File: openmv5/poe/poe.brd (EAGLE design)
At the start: 35.6 x 44.4 mm, 51 parts, among them IC1 AG9905LP, J1 GMJXHT-MM-S-88, J2 OPENMV5-BOTTOM, T1 PT61018PEL

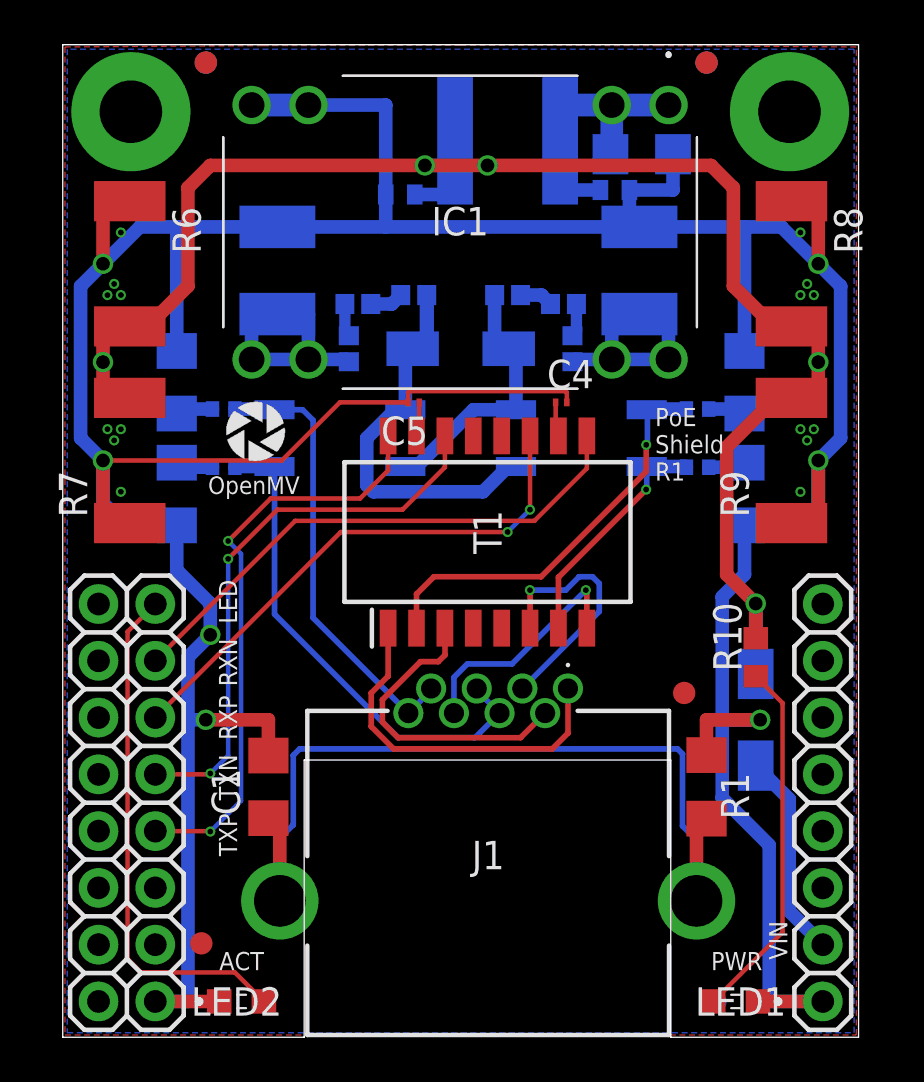
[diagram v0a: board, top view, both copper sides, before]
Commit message: Add CAN/RS232 shield
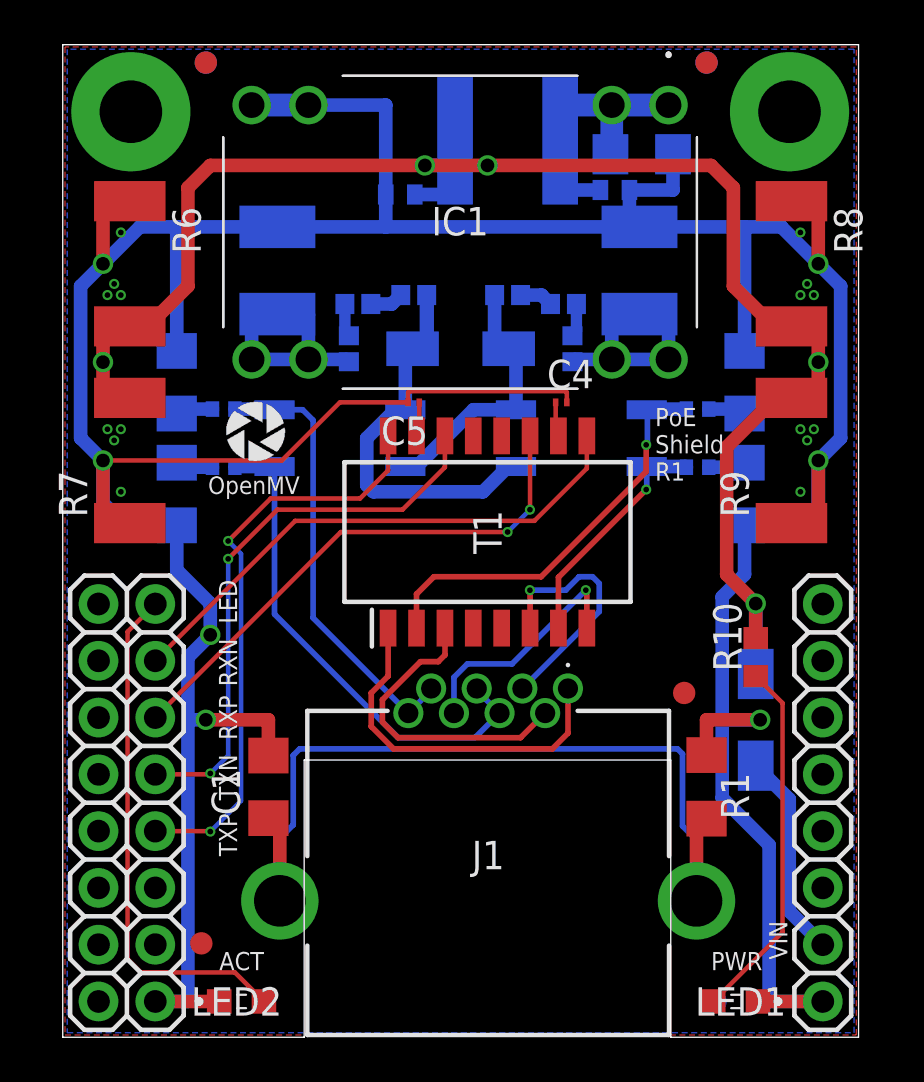
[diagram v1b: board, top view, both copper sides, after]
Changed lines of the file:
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@@
 <vertex x="0.1" y="0.1"/>
 <vertex x="35.5" y="0.1"/>
-<vertex x="35.5" y="44.3" curve="1.012964"/>
+<vertex x="35.5" y="44.3"/>
 <vertex x="0.1" y="44.3"/>
 </polygon>

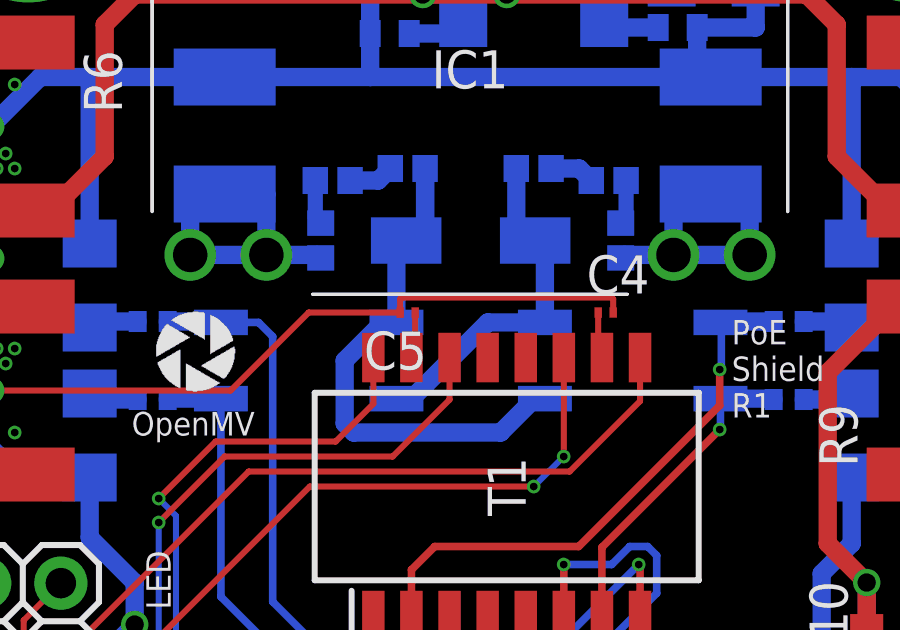
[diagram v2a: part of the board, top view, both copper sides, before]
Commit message: Remove 0201 components
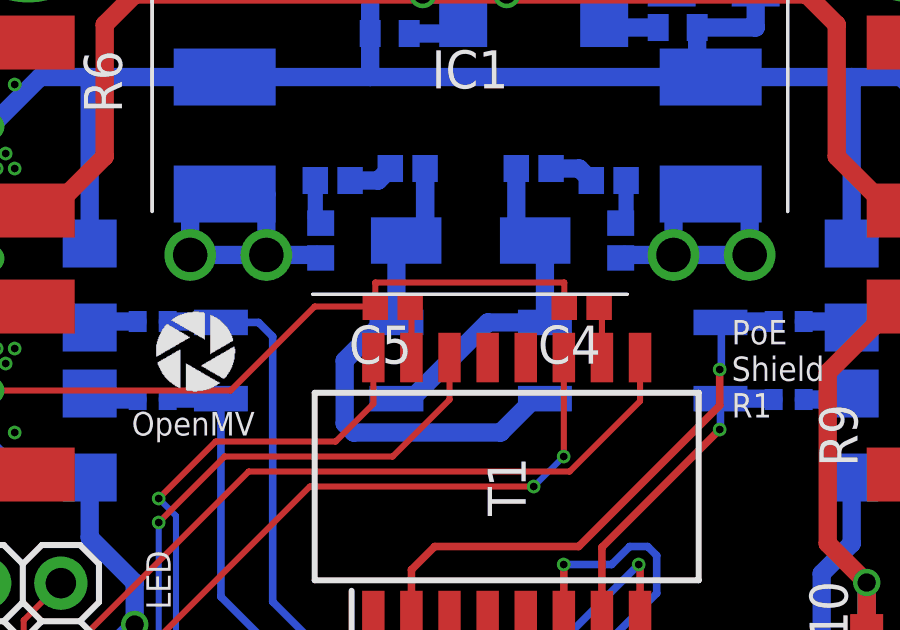
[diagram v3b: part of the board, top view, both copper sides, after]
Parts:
- C4, C5: device rcl:C0201 -> SparkFun-Capacitors:0402
- moved C4 0.82 mm to (21.5, 28.6), turned to 180 degrees
- moved C5 0.54 mm to (15.2, 28.6)
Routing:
- net GND: track 196.3 -> 195.4 mm
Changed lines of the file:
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@@
 <attribute name="VALUE" x="19" y="22.6" size="1.27" layer="27" rot="R90" align="center"/>
 </element>
-<element name="C5" library="rcl" library_urn="urn:adsk.eagle:library:334" package="C0201" package3d_urn="urn:adsk.eagle:package:23690/2" value="0.1uF" x="15.7" y="28.4" smashed="yes" rot="R180">
-<attribute name="MPN" value="CL03A104KQ3NNNC" x="15.7" y="28.4" size="1.778" layer="27" rot="R180" display="off"/>
-<attribute name="NAME" x="16.335" y="27.765" size="1.27" layer="25" rot="R180"/>
-<attribute name="POPULARITY" value="0" x="15.7" y="28.4" size="1.778" layer="27" rot="R180" display="off"/>
-<attribute name="SPICEPREFIX" value="C" x="15.7" y="28.4" size="1.778" layer="27" rot="R180" display="off"/>
-<attribute name="VALUE" x="16.335" y="30.305" size="1.27" layer="27" rot="R180"/>
-</element>
-<element name="C4" library="rcl" library_urn="urn:adsk.eagle:library:334" package="C0201" package3d_urn="urn:adsk.eagle:package:23690/2" value="0.1uF" x="22.3" y="28.4" smashed="yes">
-<attribute name="MPN" value="CL03A104KQ3NNNC" x="22.3" y="28.4" size="1.778" layer="27" display="off"/>
-<attribute name="NAME" x="21.665" y="29.035" size="1.27" layer="25"/>
-<attribute name="POPULARITY" value="0" x="22.3" y="28.4" size="1.778" layer="27" display="off"/>
-<attribute name="SPICEPREFIX" value="C" x="22.3" y="28.4" size="1.778" layer="27" display="off"/>
-<attribute name="VALUE" x="21.665" y="26.495" size="1.27" layer="27"/>
+<element name="C5" library="SparkFun-Capacitors" library_urn="urn:adsk.eagle:library:510" package="0402" package3d_urn="urn:adsk.eagle:package:37413/1" value="0.1uF" x="15.2" y="28.6" smashed="yes" rot="R180">
+<attribute name="MPN" value="GRM155R71H104KE14D" x="15.2" y="28.6" size="1.778" layer="27" rot="R180" display="off"/>
+<attribute name="NAME" x="15.835" y="27.965" size="1.27" layer="25" rot="R180"/>
+<attribute name="PROD_ID" value="CAP-12416" x="15.2" y="28.6" size="1.778" layer="27" rot="R180" display="off"/>
+<attribute name="VALUE" value="0.1uF" x="15.835" y="30.505" size="1.27" layer="27" rot="R180"/>
+</element>
+<element name="C4" library="SparkFun-Capacitors" library_urn="urn:adsk.eagle:library:510" package="0402" package3d_urn="urn:adsk.eagle:package:37413/1" value="0.1uF" x="21.5" y="28.6" smashed="yes" rot="R180">
+<attribute name="MPN" value="GRM155R71H104KE14D" x="21.5" y="28.6" size="1.778" layer="27" rot="R180" display="off"/>
+<attribute name="NAME" x="22.135" y="27.965" size="1.27" layer="25" rot="R180"/>
+<attribute name="PROD_ID" value="CAP-12416" x="21.5" y="28.6" size="1.778" layer="27" rot="R180" display="off"/>
+<attribute name="VALUE" value="0.1uF" x="22.135" y="30.505" size="1.27" layer="27" rot="R180"/>
 </element>
 <element name="BR1" library="MB6S-TP" package="SOP254P665X270-4N" value="MB6S-TP" x="23.2" y="26.8" smashed="yes" rot="MR0">
@@
 <wire x1="29.5" y1="10.7" x2="31.6" y2="8.6" width="0.6096" layer="16"/>
 <wire x1="1.8" y1="25.8" x2="9.8" y2="25.8" width="0.2032" layer="1"/>
-<wire x1="9.8" y1="25.8" x2="12.4" y2="28.4" width="0.2032" layer="1"/>
-<wire x1="12.4" y1="28.4" x2="15.45" y2="28.4" width="0.2032" layer="1"/>
-<wire x1="22.55" y1="28.4" x2="22.55" y2="28.85" width="0.2032" layer="1"/>
-<wire x1="22.55" y1="28.85" x2="22.5" y2="28.9" width="0.2032" layer="1"/>
-<wire x1="22.5" y1="28.9" x2="15.5" y2="28.9" width="0.2032" layer="1"/>
-<wire x1="15.45" y1="28.85" x2="15.45" y2="28.4" width="0.2032" layer="1"/>
-<wire x1="15.5" y1="28.9" x2="15.45" y2="28.85" width="0.2032" layer="1"/>
+<wire x1="9.8" y1="25.8" x2="12.6" y2="28.6" width="0.2032" layer="1"/>
+<wire x1="12.6" y1="28.6" x2="14.62" y2="28.6" width="0.2032" layer="1"/>
+<wire x1="20.92" y1="28.6" x2="20.92" y2="29.4" width="0.2032" layer="1"/>
+<wire x1="20.92" y1="29.4" x2="14.62" y2="29.4" width="0.2032" layer="1"/>
+<wire x1="14.62" y1="28.6" x2="14.62" y2="29.4" width="0.2032" layer="1"/>
 <via x="6.6" y="18" extent="1-16" drill="0.6096"/>
 <contactref element="C1" pad="2"/>
@@
 <contactref element="T1" pad="15"/>
 <contactref element="C5" pad="1"/>
-<wire x1="15.95" y1="28.4" x2="15.95" y2="27.025" width="0.2032" layer="1"/>
-<wire x1="15.95" y1="27.025" x2="15.825" y2="26.9" width="0.2032" layer="1"/>
+<wire x1="15.78" y1="28.6" x2="15.625" y2="28.6" width="0.2032" layer="1"/>
+<wire x1="15.825" y1="26.9" x2="15.825" y2="28.4" width="0.2032" layer="1"/>
+<wire x1="15.825" y1="28.4" x2="15.625" y2="28.6" width="0.2032" layer="1"/>
 </signal>
 <signal name="MDI_RX_CT" class="3">
 <contactref element="T1" pad="10"/>
 <contactref element="C4" pad="1"/>
-<wire x1="22.05" y1="28.4" x2="22.05" y2="27.025" width="0.2032" layer="1"/>
-<wire x1="22.05" y1="27.025" x2="22.175" y2="26.9" width="0.2032" layer="1"/>
+<wire x1="22.08" y1="28.6" x2="22.063075" y2="28.616925" width="0.2032" layer="1"/>
+<wire x1="22.063075" y1="28.616925" x2="22.057625" y2="28.617375" width="0.2032" layer="1"/>
+<wire x1="22.175" y1="28.5" x2="22.175" y2="26.9" width="0.2032" layer="1"/>
+<wire x1="22.175" y1="28.5" x2="22.057625" y2="28.617375" width="0.2032" layer="1"/>
 </signal>
 <signal name="TX_N" class="4">

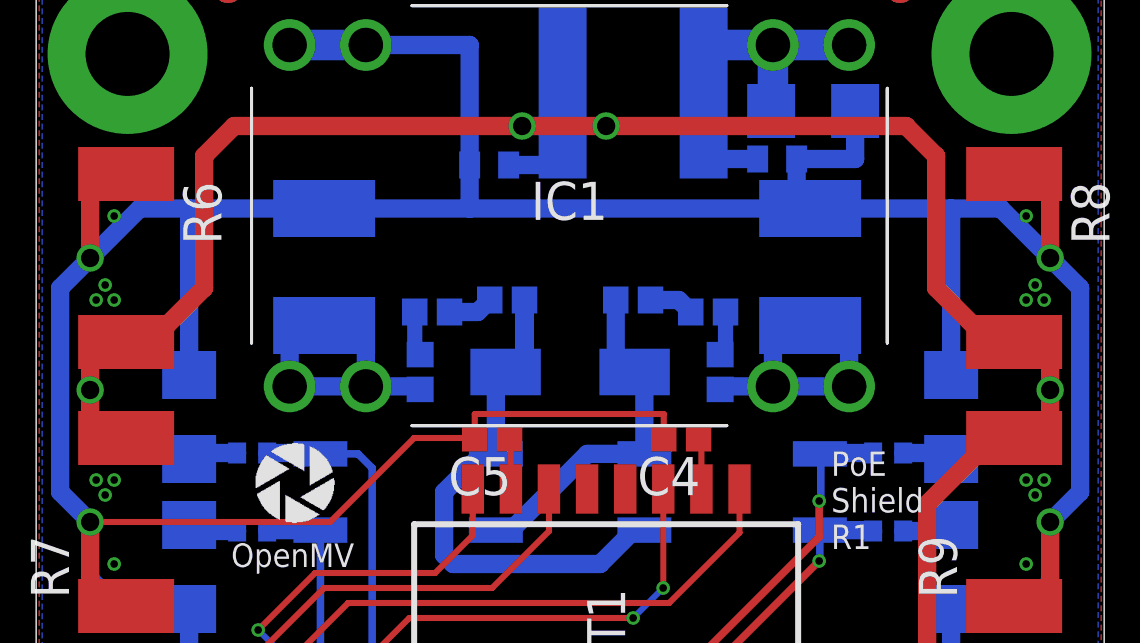
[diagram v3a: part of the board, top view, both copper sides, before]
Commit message: Fix inductor size
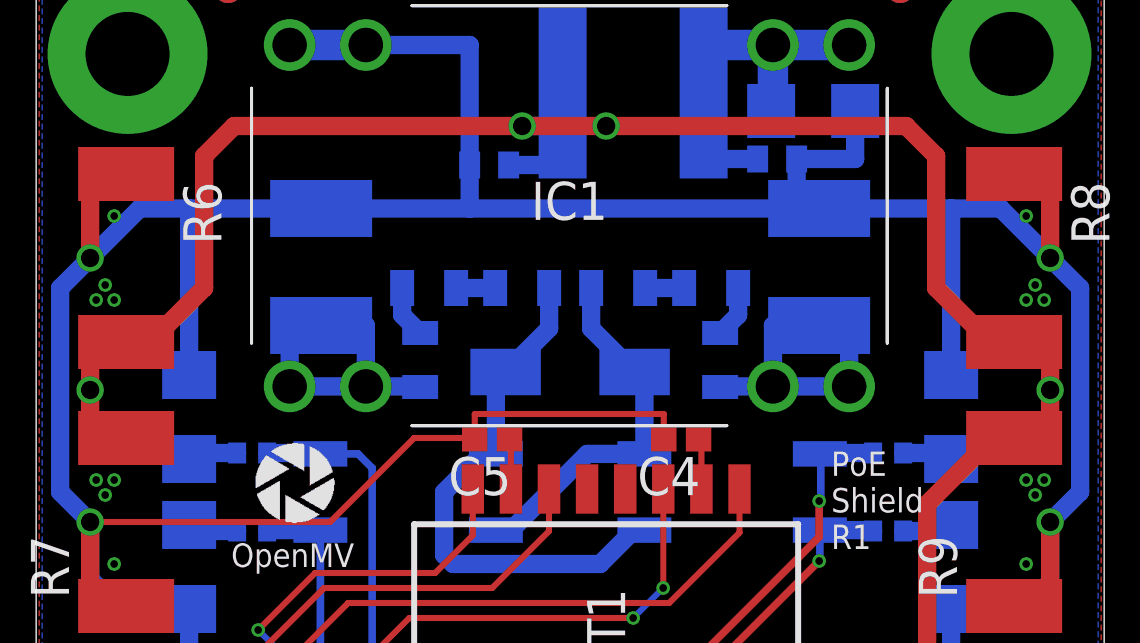
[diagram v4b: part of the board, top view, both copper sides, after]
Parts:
- L1, L2, L3, L4, L5, L6: value 1k -> 1K; device SparkFun-Coils:0402 -> SparkFun-Coils:0805
- moved L3 0.81 mm to (22.5, 33.6)
- moved L4 0.81 mm to (13.1, 33.6)
- moved L1 0.64 mm to (19.4, 33.6)
- moved L2 0.64 mm to (16.2, 33.6)
- moved L5 0.40 mm to (22.8, 31.2)
- moved L6 0.40 mm to (12.8, 31.2)
- moved C2 0.30 mm to (26.1, 34.3)
- moved C3 0.10 mm to (9.50, 34.3)
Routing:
- net POE_VIN_P: track 20.3 -> 17.7 mm

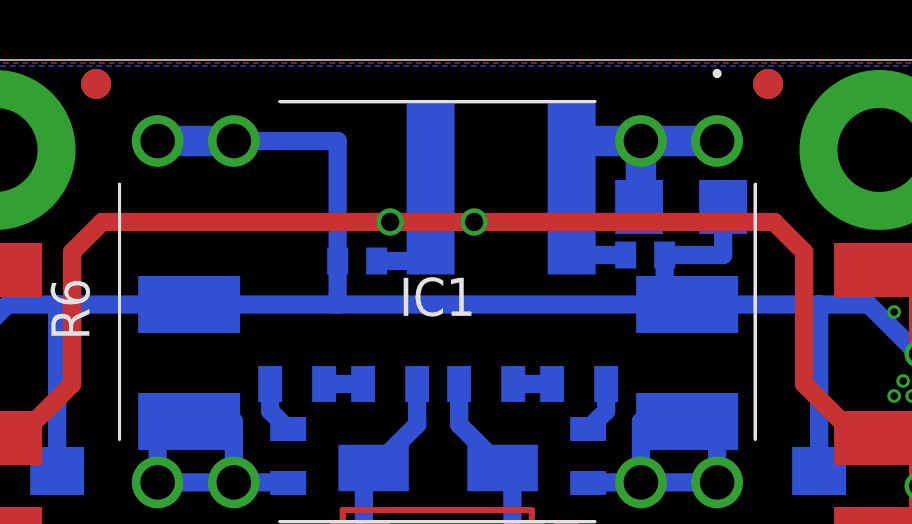
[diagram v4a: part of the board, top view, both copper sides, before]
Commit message: Change inductor to something smaller
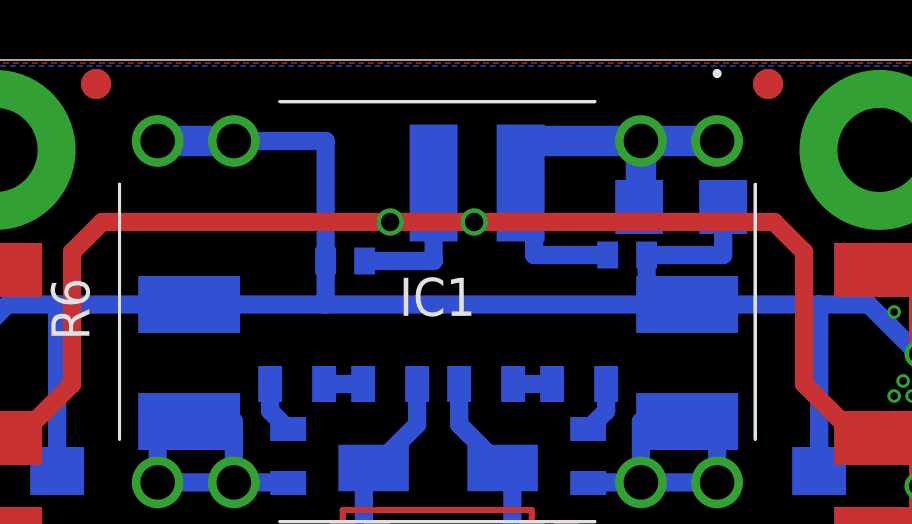
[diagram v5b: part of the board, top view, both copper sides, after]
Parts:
- L7: value NR6045T1R8N -> VLCF4020T-1R8N1R9; device NR6045T1R8N:NR6045T1R8N -> VLCF4020T-1R8N1R9:VLCF4020
- moved L7 0.82 mm to (19.1, 40.3)
- moved C7 0.60 mm to (24.1, 37.9)
- moved C11 0.40 mm to (14.7, 37.7)
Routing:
- net VIN: track 74.6 -> 76.8 mm
- net VDC: track 13.5 -> 15.3 mm
- net GND: track 195.7 -> 196.5 mm
